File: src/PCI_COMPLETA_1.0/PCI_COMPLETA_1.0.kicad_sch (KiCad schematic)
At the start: 46 parts, among them J1 USB_B_Micro, J2 Conn_01x06_Socket, J3 USB_B_Micro, J4 Screw_Terminal_01x02, J5 Screw terminal for switch, Q1 FS8205, SW1 RESET1, SW2 BOOT1, U1 ESP32-S3-MINI-1, U2 MPU-9250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

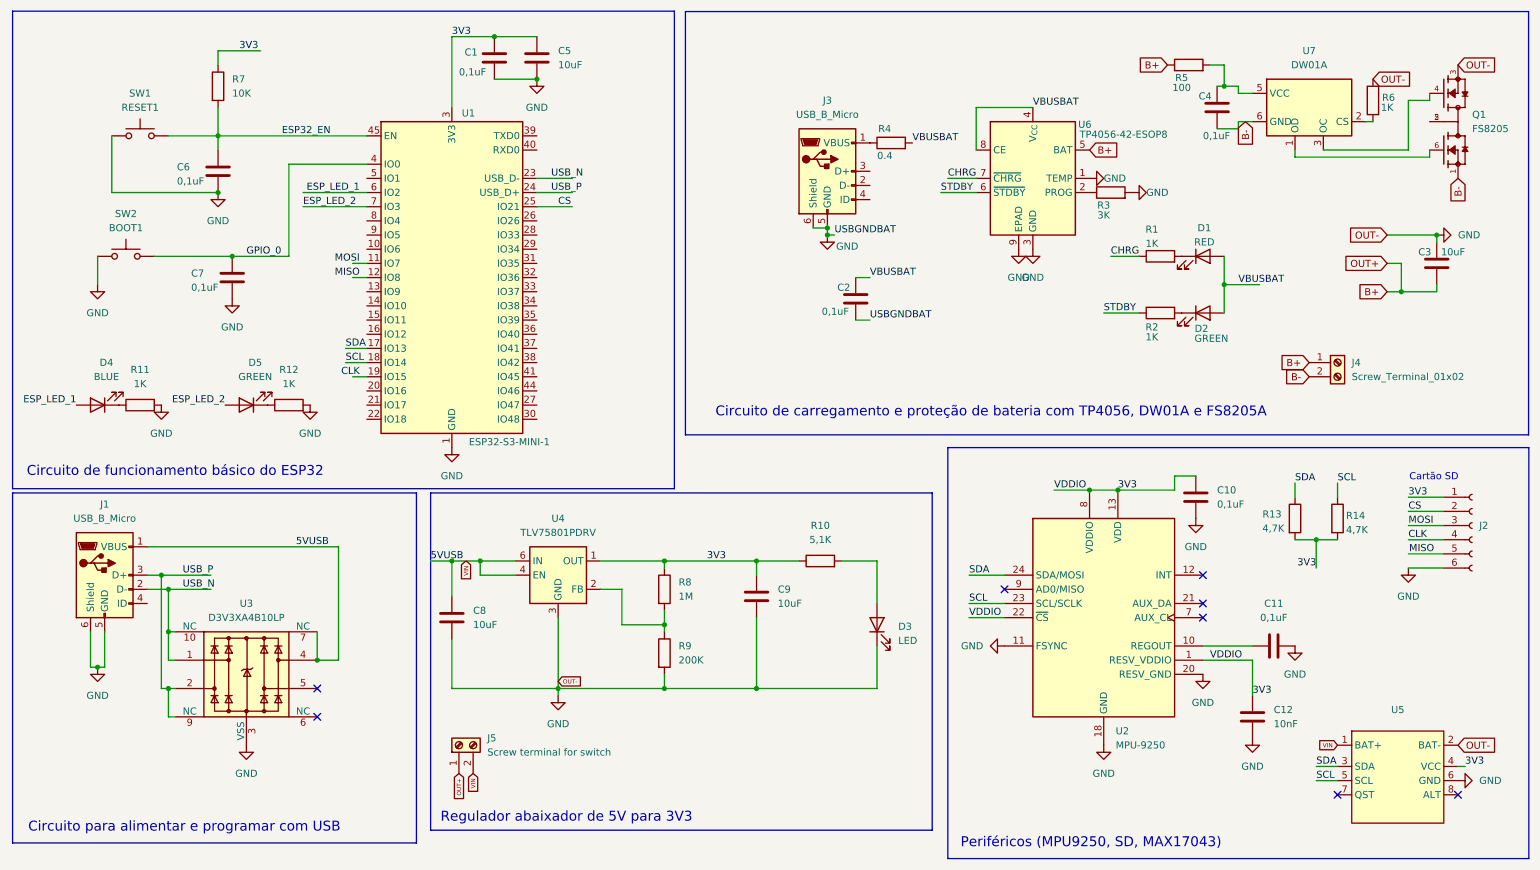
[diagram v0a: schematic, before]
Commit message: fix: corrige envio de valores de angulo
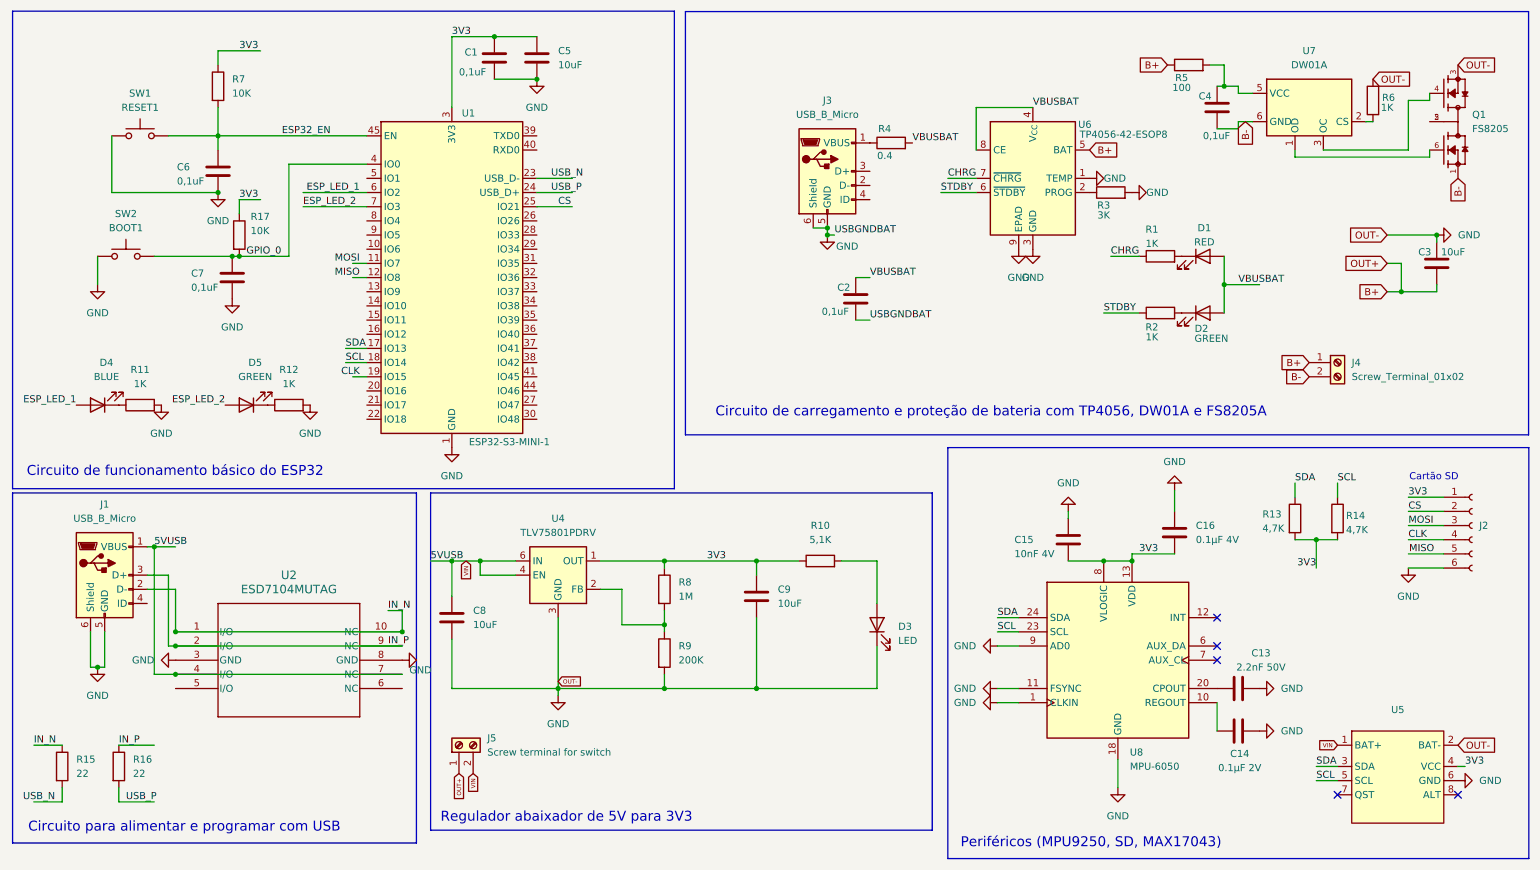
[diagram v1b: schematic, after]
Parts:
- removed C10, C11: 0,1uF, Capacitor_SMD:C_0603_1608Metric, symbol Device:C
- removed C12: 10nF, Capacitor_SMD:C_0603_1608Metric, symbol Device:C
- removed U2: MPU-9250, Sensor_Motion:InvenSense_QFN-24_3x3mm_P0.4mm, symbol Sensor_Motion:MPU-9250
- removed U3: D3V3XA4B10LP, Package_DFN_QFN:Diodes_UDFN-10_1.0x2.5mm_P0.5mm, symbol Power_Protection:D3V3XA4B10LP
- added C13: 2.2nF 50V, Capacitor_SMD:C_0603_1608Metric, symbol Device:C
- added C14: 0.1µF 2V, Capacitor_SMD:C_0603_1608Metric, symbol Device:C
- added C15: 10nF 4V, Capacitor_SMD:C_0603_1608Metric, symbol Device:C
- added C16: 0.1µF 4V, Capacitor_SMD:C_0603_1608Metric, symbol Device:C
- added R15, R16: 22, Resistor_SMD:R_0402_1005Metric, symbol Device:R
- added R17: 10K, Resistor_SMD:R_0603_1608Metric, symbol Device:R
- added U2: ESD7104MUTAG, UDFN10_ONS, symbol MUTAG:ESD7104MUTAG
- added U8: MPU-6050, Sensor_Motion:InvenSense_QFN-24_4x4mm_P0.5mm, symbol Sensor_Motion:MPU-6050
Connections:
- net 3V3: now also C15.2, C16.2, R17.1, U8.13 (VDD), U8.8 (VLOGIC)
- net GND: now also C13.1, C14.1, C15.1, C16.1, U2.3 (GND), U2.8 (GND), U8.1 (CLKIN), U8.11 (FSYNC), U8.18 (GND), U8.9 (AD0)
- net GPIO_0: now also R17.2
- net SCL: now also U8.23 (SCL)
- net SDA: now also U8.24 (SDA)
- net USB_N: now also R15.2; no longer J1.2 (D-)
- net USB_P: now also R16.2; no longer J1.3 (D+)
- net VIN: now also U2.4 (I/O), U2.7 (NC)
- new net: C13.2, U8.20 (CPOUT)
- new net: C14.2, U8.10 (REGOUT)
- new net IN_N: J1.2 (D-), R15.1, U2.1 (I/O), U2.10 (NC)
- new net IN_P: J1.3 (D+), R16.1, U2.2 (I/O), U2.9 (NC)
- no-connect marks 8 -> 5
